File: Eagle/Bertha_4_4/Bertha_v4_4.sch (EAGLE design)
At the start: 115 parts, among them CON1 JACK_DC_BARREL, CON2 JACK_DC_BARREL, IC1 MCP1703DB, J1 RJ12RIGHTANGLE-I2C, J2 RJ12RIGHTANGLE-I2C, Q1 BSP75, Q2 BSP75, Q3 BSP75, Q4 BSP75, Q5 BSP75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

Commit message: Changed DS18B20 package to MSOP8
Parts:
- removed U$4: DS18B20, lpatiny:DS18B20
- added U$2: DS18B20SMALL, lpatiny:DS18B20SMALL
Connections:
- net 3.3V: now also U$2.VDD; no longer U$4.VDD
- net GND: now also U$2.GND; no longer U$4.GND
- net N$9: now also U$2.DQ; no longer U$4.DQ
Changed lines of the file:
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@@
 <grid distance="0.1" unitdist="inch" unit="inch" style="lines" multiple="1" display="no" altdistance="0.01" altunitdist="inch" altunit="inch"/>
 <layers>
-<layer number="1" name="Top" color="4" fill="1" visible="no" active="no"/>
-<layer number="16" name="Bottom" color="1" fill="1" visible="no" active="no"/>
-<layer number="17" name="Pads" color="2" fill="1" visible="no" active="no"/>
-<layer number="18" name="Vias" color="2" fill="1" visible="no" active="no"/>
-<layer number="19" name="Unrouted" color="6" fill="1" visible="no" active="no"/>
-<layer number="20" name="Dimension" color="15" fill="1" visible="no" active="no"/>
-<layer number="21" name="tPlace" color="7" fill="1" visible="no" active="no"/>
-<layer number="22" name="bPlace" color="7" fill="1" visible="no" active="no"/>
-<layer number="23" name="tOrigins" color="15" fill="1" visible="no" active="no"/>
-<layer number="24" name="bOrigins" color="15" fill="1" visible="no" active="no"/>
-<layer number="25" name="tNames" color="7" fill="1" visible="no" active="no"/>
-<layer number="26" name="bNames" color="7" fill="1" visible="no" active="no"/>
-<layer number="27" name="tValues" color="7" fill="1" visible="no" active="no"/>
-<layer number="28" name="bValues" color="7" fill="1" visible="no" active="no"/>
+<layer number="1" name="Top" color="4" fill="1" visible="yes" active="no"/>
+<layer number="16" name="Bottom" color="1" fill="1" visible="yes" active="no"/>
+<layer number="17" name="Pads" color="2" fill="1" visible="yes" active="no"/>
+<layer number="18" name="Vias" color="2" fill="1" visible="yes" active="no"/>
+<layer number="19" name="Unrouted" color="6" fill="1" visible="yes" active="no"/>
+<layer number="20" name="Dimension" color="15" fill="1" visible="yes" active="no"/>
+<layer number="21" name="tPlace" color="7" fill="1" visible="yes" active="no"/>
+<layer number="22" name="bPlace" color="7" fill="1" visible="yes" active="no"/>
+<layer number="23" name="tOrigins" color="15" fill="1" visible="yes" active="no"/>
+<layer number="24" name="bOrigins" color="15" fill="1" visible="yes" active="no"/>
+<layer number="25" name="tNames" color="7" fill="1" visible="yes" active="no"/>
+<layer number="26" name="bNames" color="7" fill="1" visible="yes" active="no"/>
+<layer number="27" name="tValues" color="7" fill="1" visible="yes" active="no"/>
+<layer number="28" name="bValues" color="7" fill="1" visible="yes" active="no"/>
 <layer number="29" name="tStop" color="7" fill="3" visible="no" active="no"/>
 <layer number="30" name="bStop" color="7" fill="6" visible="no" active="no"/>
@@
 <layer number="35" name="tGlue" color="7" fill="4" visible="no" active="no"/>
 <layer number="36" name="bGlue" color="7" fill="5" visible="no" active="no"/>
-<layer number="37" name="tTest" color="7" fill="1" visible="no" active="no"/>
-<layer number="38" name="bTest" color="7" fill="1" visible="no" active="no"/>
+<layer number="37" name="tTest" color="7" fill="1" visible="yes" active="no"/>
+<layer number="38" name="bTest" color="7" fill="1" visible="yes" active="no"/>
 <layer number="39" name="tKeepout" color="4" fill="11" visible="no" active="no"/>
 <layer number="40" name="bKeepout" color="1" fill="11" visible="no" active="no"/>
@@
 <layer number="44" name="Drills" color="7" fill="1" visible="no" active="no"/>
 <layer number="45" name="Holes" color="7" fill="1" visible="no" active="no"/>
-<layer number="46" name="Milling" color="3" fill="1" visible="no" active="no"/>
-<layer number="47" name="Measures" color="7" fill="1" visible="no" active="no"/>
-<layer number="48" name="Document" color="7" fill="1" visible="no" active="no"/>
-<layer number="49" name="Reference" color="7" fill="1" visible="no" active="no"/>
-<layer number="50" name="dxf" color="12" fill="1" visible="no" active="no"/>
-<layer number="51" name="tDocu" color="7" fill="1" visible="no" active="no"/>
-<layer number="52" name="bDocu" color="7" fill="1" visible="no" active="no"/>
-<layer number="53" name="tGND_GNDA" color="7" fill="1" visible="no" active="no"/>
-<layer number="54" name="bGND_GNDA" color="7" fill="1" visible="no" active="no"/>
-<layer number="56" name="wert" color="7" fill="1" visible="no" active="no"/>
-<layer number="57" name="tCAD" color="7" fill="1" visible="no" active="no"/>
-<layer number="59" name="tCarbon" color="7" fill="1" visible="no" active="no"/>
-<layer number="60" name="bCarbon" color="7" fill="1" visible="no" active="no"/>
+<layer number="46" name="Milling" color="3" fill="1" visible="yes" active="no"/>
+<layer number="47" name="Measures" color="7" fill="1" visible="yes" active="no"/>
+<layer number="48" name="Document" color="7" fill="1" visible="yes" active="no"/>
+<layer number="49" name="Reference" color="7" fill="1" visible="yes" active="no"/>
+<layer number="50" name="dxf" color="12" fill="1" visible="yes" active="no"/>
+<layer number="51" name="tDocu" color="7" fill="1" visible="yes" active="no"/>
+<layer number="52" name="bDocu" color="7" fill="1" visible="yes" active="no"/>
+<layer number="53" name="tGND_GNDA" color="7" fill="1" visible="yes" active="no"/>
+<layer number="54" name="bGND_GNDA" color="7" fill="1" visible="yes" active="no"/>
+<layer number="56" name="wert" color="7" fill="1" visible="yes" active="no"/>
+<layer number="57" name="tCAD" color="7" fill="1" visible="yes" active="no"/>
+<layer number="59" name="tCarbon" color="7" fill="1" visible="yes" active="no"/>
+<layer number="60" name="bCarbon" color="7" fill="1" visible="yes" active="no"/>
 <layer number="90" name="Modules" color="5" fill="1" visible="no" active="no"/>
 <layer number="91" name="Nets" color="2" fill="1" visible="yes" active="yes"/>
@@
 <part name="GND17" library="supply1" deviceset="GND" device=""/>
 <part name="GND18" library="supply1" deviceset="GND" device=""/>
-<part name="U$4" library="lpatiny" deviceset="DS18B20" device=""/>
 <part name="J1" library="lpatiny" deviceset="RJ12" device="RIGHTANGLE-I2C"/>
 <part name="J2" library="lpatiny" deviceset="RJ12" device="RIGHTANGLE-I2C"/>
@@
 <part name="CON2" library="lpatiny" deviceset="JACK_DC_BARREL" device=""/>
 <part name="X1" library="con-lumberg" deviceset="1503_09" device=""/>
+<part name="U$2" library="lpatiny" deviceset="DS18B20" device="SMALL"/>
 </parts>
 <sheets>
@@
 <instance part="GND17" gate="1" x="345.44" y="231.14"/>
 <instance part="GND18" gate="1" x="337.82" y="236.22"/>
-<instance part="U$4" gate="G$1" x="297.18" y="22.86"/>
 <instance part="J1" gate="G$1" x="368.3" y="271.78"/>
 <instance part="J2" gate="G$1" x="368.3" y="241.3"/>
@@
 <instance part="CON2" gate="G$1" x="367.538" y="44.45" rot="R90"/>
 <instance part="X1" gate="G$1" x="284.48" y="43.18" rot="MR180"/>
+<instance part="U$2" gate="G$1" x="297.18" y="22.86"/>
 </instances>
 <busses>
@@
 <segment>
 <pinref part="GND20" gate="1" pin="GND"/>
-<pinref part="U$4" gate="G$1" pin="GND"/>
 <wire x1="312.42" y1="20.32" x2="307.34" y2="20.32" width="0.1524" layer="91"/>
+<pinref part="U$2" gate="G$1" pin="GND"/>
 </segment>
 <segment>
@@
 <wire x1="274.32" y1="22.86" x2="274.32" y2="27.94" width="0.1524" layer="91"/>
 <junction x="274.32" y="22.86"/>
-<pinref part="U$4" gate="G$1" pin="VDD"/>
 <wire x1="284.48" y1="22.86" x2="274.32" y2="22.86" width="0.1524" layer="91"/>
 <pinref part="P+36" gate="G$1" pin="3.3V"/>
+<pinref part="U$2" gate="G$1" pin="VDD"/>
 </segment>
 <segment>
@@
 <pinref part="R10" gate="G$1" pin="2"/>
 <junction x="264.16" y="20.32"/>
-<pinref part="U$4" gate="G$1" pin="DQ"/>
+<pinref part="U$2" gate="G$1" pin="DQ"/>
 </segment>
 </net>

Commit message: regenerated gerbers for 4.4, displaying values
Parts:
- 12V: value (none) -> 12V
- BKLD: value RED -> BLK
- C1, C10, C11, C12, C13, C2, C3, C4, C5, C6, C7, C8, C9: value 100nF -> 100n
- CU1, CU2, CU3, CU4, CU7, CU8: value 10uF -> 10u
- GND: value (none) -> GND
- LDMEM: value RED -> Flash
- LDSLAVE: value RED -> LCD
- R12: value 1k -> 10k
- R2, RK14, RK15, RK16, RK18: value 10k -> 1k
- RXLD: value RED -> RX
- TX: value RED -> TX
- U$2: value DS18B20SMALL -> DS18B20
- renumbered TXLD to TX

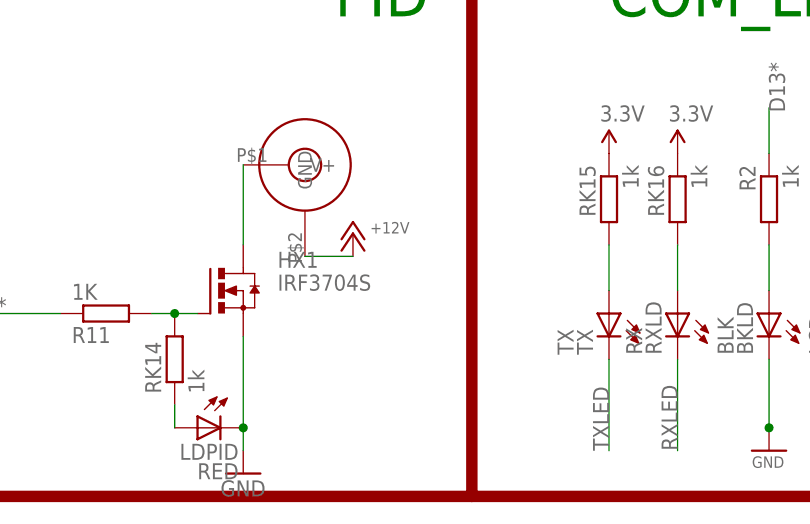
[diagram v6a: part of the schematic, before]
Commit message: changed PID FET part, ref #72
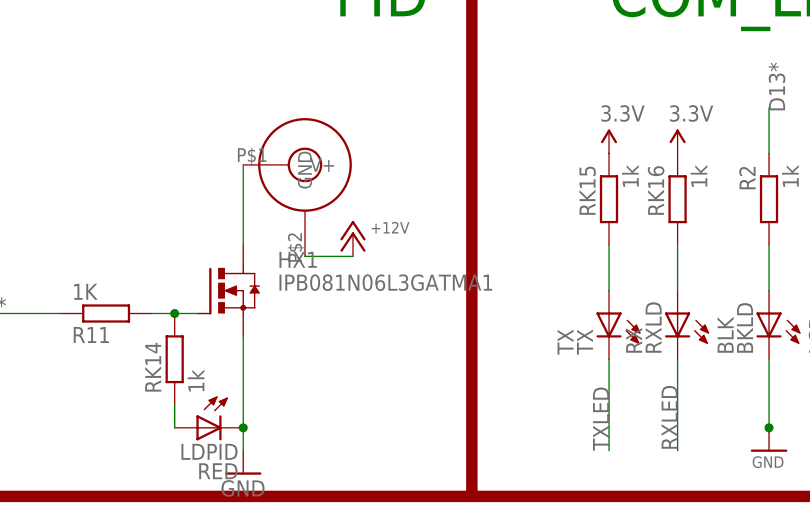
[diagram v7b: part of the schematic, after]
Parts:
- HX1: value IRF3704S -> IPB081N06L3GATMA1
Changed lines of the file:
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@@
 <grid distance="0.1" unitdist="inch" unit="inch" style="lines" multiple="1" display="no" altdistance="0.01" altunitdist="inch" altunit="inch"/>
 <layers>
-<layer number="1" name="Top" color="4" fill="1" visible="yes" active="no"/>
-<layer number="16" name="Bottom" color="1" fill="1" visible="yes" active="no"/>
-<layer number="17" name="Pads" color="2" fill="1" visible="yes" active="no"/>
-<layer number="18" name="Vias" color="2" fill="1" visible="yes" active="no"/>
-<layer number="19" name="Unrouted" color="6" fill="1" visible="yes" active="no"/>
-<layer number="20" name="Dimension" color="15" fill="1" visible="yes" active="no"/>
-<layer number="21" name="tPlace" color="7" fill="1" visible="yes" active="no"/>
-<layer number="22" name="bPlace" color="7" fill="1" visible="yes" active="no"/>
-<layer number="23" name="tOrigins" color="15" fill="1" visible="yes" active="no"/>
-<layer number="24" name="bOrigins" color="15" fill="1" visible="yes" active="no"/>
-<layer number="25" name="tNames" color="7" fill="1" visible="yes" active="no"/>
-<layer number="26" name="bNames" color="7" fill="1" visible="yes" active="no"/>
-<layer number="27" name="tValues" color="7" fill="1" visible="yes" active="no"/>
-<layer number="28" name="bValues" color="7" fill="1" visible="yes" active="no"/>
+<layer number="1" name="Top" color="4" fill="1" visible="no" active="no"/>
+<layer number="16" name="Bottom" color="1" fill="1" visible="no" active="no"/>
+<layer number="17" name="Pads" color="2" fill="1" visible="no" active="no"/>
+<layer number="18" name="Vias" color="2" fill="1" visible="no" active="no"/>
+<layer number="19" name="Unrouted" color="6" fill="1" visible="no" active="no"/>
+<layer number="20" name="Dimension" color="15" fill="1" visible="no" active="no"/>
+<layer number="21" name="tPlace" color="7" fill="1" visible="no" active="no"/>
+<layer number="22" name="bPlace" color="7" fill="1" visible="no" active="no"/>
+<layer number="23" name="tOrigins" color="15" fill="1" visible="no" active="no"/>
+<layer number="24" name="bOrigins" color="15" fill="1" visible="no" active="no"/>
+<layer number="25" name="tNames" color="7" fill="1" visible="no" active="no"/>
+<layer number="26" name="bNames" color="7" fill="1" visible="no" active="no"/>
+<layer number="27" name="tValues" color="7" fill="1" visible="no" active="no"/>
+<layer number="28" name="bValues" color="7" fill="1" visible="no" active="no"/>
 <layer number="29" name="tStop" color="7" fill="3" visible="no" active="no"/>
 <layer number="30" name="bStop" color="7" fill="6" visible="no" active="no"/>
@@
 <layer number="35" name="tGlue" color="7" fill="4" visible="no" active="no"/>
 <layer number="36" name="bGlue" color="7" fill="5" visible="no" active="no"/>
-<layer number="37" name="tTest" color="7" fill="1" visible="yes" active="no"/>
-<layer number="38" name="bTest" color="7" fill="1" visible="yes" active="no"/>
+<layer number="37" name="tTest" color="7" fill="1" visible="no" active="no"/>
+<layer number="38" name="bTest" color="7" fill="1" visible="no" active="no"/>
 <layer number="39" name="tKeepout" color="4" fill="11" visible="no" active="no"/>
 <layer number="40" name="bKeepout" color="1" fill="11" visible="no" active="no"/>
@@
 <layer number="44" name="Drills" color="7" fill="1" visible="no" active="no"/>
 <layer number="45" name="Holes" color="7" fill="1" visible="no" active="no"/>
-<layer number="46" name="Milling" color="3" fill="1" visible="yes" active="no"/>
-<layer number="47" name="Measures" color="7" fill="1" visible="yes" active="no"/>
-<layer number="48" name="Document" color="7" fill="1" visible="yes" active="no"/>
-<layer number="49" name="Reference" color="7" fill="1" visible="yes" active="no"/>
-<layer number="50" name="dxf" color="12" fill="1" visible="yes" active="no"/>
-<layer number="51" name="tDocu" color="7" fill="1" visible="yes" active="no"/>
-<layer number="52" name="bDocu" color="7" fill="1" visible="yes" active="no"/>
-<layer number="53" name="tGND_GNDA" color="7" fill="1" visible="yes" active="no"/>
-<layer number="54" name="bGND_GNDA" color="7" fill="1" visible="yes" active="no"/>
-<layer number="56" name="wert" color="7" fill="1" visible="yes" active="no"/>
-<layer number="57" name="tCAD" color="7" fill="1" visible="yes" active="no"/>
-<layer number="59" name="tCarbon" color="7" fill="1" visible="yes" active="no"/>
-<layer number="60" name="bCarbon" color="7" fill="1" visible="yes" active="no"/>
+<layer number="46" name="Milling" color="3" fill="1" visible="no" active="no"/>
+<layer number="47" name="Measures" color="7" fill="1" visible="no" active="no"/>
+<layer number="48" name="Document" color="7" fill="1" visible="no" active="no"/>
+<layer number="49" name="Reference" color="7" fill="1" visible="no" active="no"/>
+<layer number="50" name="dxf" color="12" fill="1" visible="no" active="no"/>
+<layer number="51" name="tDocu" color="7" fill="1" visible="no" active="no"/>
+<layer number="52" name="bDocu" color="7" fill="1" visible="no" active="no"/>
+<layer number="53" name="tGND_GNDA" color="7" fill="1" visible="no" active="no"/>
+<layer number="54" name="bGND_GNDA" color="7" fill="1" visible="no" active="no"/>
+<layer number="56" name="wert" color="7" fill="1" visible="no" active="no"/>
+<layer number="57" name="tCAD" color="7" fill="1" visible="no" active="no"/>
+<layer number="59" name="tCarbon" color="7" fill="1" visible="no" active="no"/>
+<layer number="60" name="bCarbon" color="7" fill="1" visible="no" active="no"/>
 <layer number="90" name="Modules" color="5" fill="1" visible="no" active="no"/>
 <layer number="91" name="Nets" color="2" fill="1" visible="yes" active="yes"/>
@@
 <part name="GND8" library="supply1" deviceset="GND" device=""/>
 <part name="GND27" library="supply1" deviceset="GND" device=""/>
-<part name="HX1" library="transistor-power" deviceset="IRF3704" device="S"/>
+<part name="HX1" library="transistor-power" deviceset="IRF3704" device="S" value="IPB081N06L3GATMA1"/>
 <part name="R11" library="rcl" deviceset="R-EU_" device="R0805" value="1K"/>
 <part name="P+2" library="supply1" deviceset="+12V" device=""/>

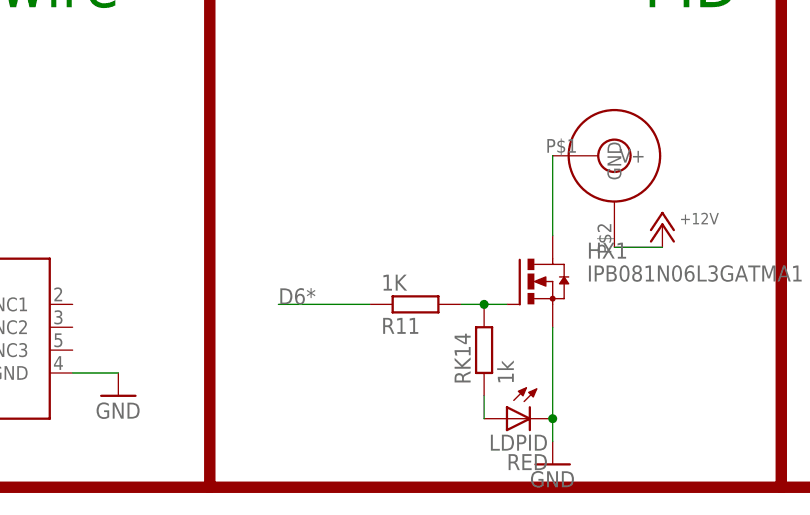
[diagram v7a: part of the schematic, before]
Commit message: correction on PID labelling, closes #71
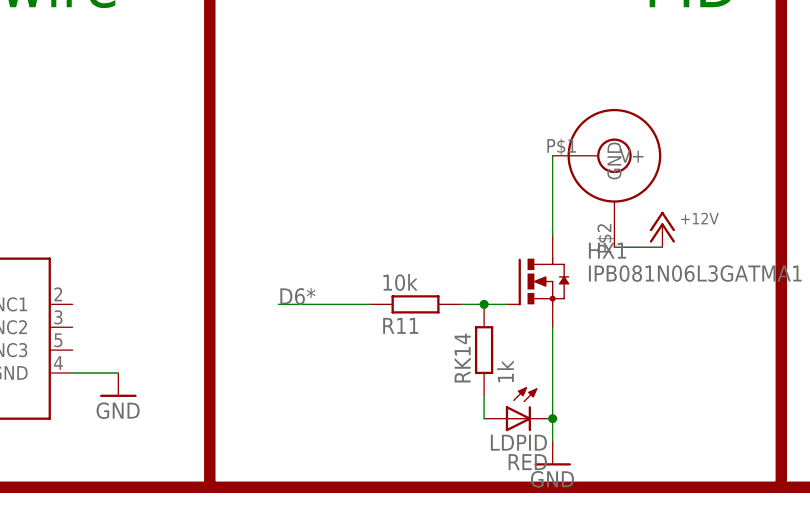
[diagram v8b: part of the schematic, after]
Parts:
- R11: value 1K -> 10k
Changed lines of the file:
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@@
 <part name="GND27" library="supply1" deviceset="GND" device=""/>
 <part name="HX1" library="transistor-power" deviceset="IRF3704" device="S" value="IPB081N06L3GATMA1"/>
-<part name="R11" library="rcl" deviceset="R-EU_" device="R0805" value="1K"/>
+<part name="R11" library="rcl" deviceset="R-EU_" device="R0805" value="10k"/>
 <part name="P+2" library="supply1" deviceset="+12V" device=""/>
 <part name="GND2" library="supply1" deviceset="GND" device=""/>
